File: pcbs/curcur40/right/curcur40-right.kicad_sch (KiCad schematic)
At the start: 88 parts, among them U1 PMW3360, U2 TLV74318PDBVR

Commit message: fix(pcb): eliminate all ERC/DRC/parity warnings and ignored DRC checks on left and right PCBs
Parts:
- U1: value PMW3360 -> PMW3360DM-T2QU; Mfr. # PMW3360DM-T2QU + LM19-LSI -> (none)
- rEXSW1: now left out of the parts list
- rLED9: footprint kbd_local:YS-SK6812MINI-E -> kbd_local:YS-SK6812MINI-E_rLED9
- rSW1: footprint kbd_local:keyswitch_choc12_hotswap_1u -> kbd_local:keyswitch_choc12_hotswap_1.5u
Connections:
- net +1V8_PMW: now also C1.1, C2.1, U1.3 (VDDPIX)
- net MOTION: no longer names the net of U1.9 (MOTION)
- no-connect marks 3 -> 4

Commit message: Refactor PCBs and schematics to use genuine KiCad 10.0 standard libraries and isolate PMW3360 VDDPIX
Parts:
- U1: footprint kbd_local:PMW3360DM-T2QU_16Pin -> kbd:PMW3360DM-T2QU_16Pin
- rEXLED2, rLED1, rLED10, rLED11, rLED12, rLED13, rLED14, rLED15, rLED16, rLED17, rLED18, rLED2, rLED3, rLED4, rLED5, rLED6, rLED7, rLED8: footprint kbd_local:YS-SK6812MINI-E -> kbd:YS-SK6812MINI-E; symbol kbd_local:YS-SK6812MINI-E -> kbd:YS-SK6812MINI-E
- rEXSW1: footprint kbd_local:CKW12 -> kbd:RotaryEncoder_Switch_CKW12
- rEXSW2, rSW10, rSW11, rSW12, rSW13, rSW14, rSW15, rSW16, rSW17, rSW18, rSW2, rSW3, rSW4, rSW5, rSW6, rSW7, rSW8, rSW9: footprint kbd_local:keyswitch_choc12_hotswap_1u -> kbd:keyswitch_choc12_hotswap_1u
- rJ1: footprint kbd_local:TYPE-C-31-M-13C -> kbd:USB_C_Receptacle_TYPE-C-31-M-13C; symbol Connector:USB_C_Receptacle_USB2.0 -> Connector:USB_C_Receptacle_USB2.0_16P
- rJ2: footprint kbd_local:PJ-398A-5A_PJ-399B-6A -> kbd:Jack_PJ-398A-5A_PJ-399B-6A
- rLED9: footprint kbd_local:YS-SK6812MINI-E_rLED9 -> kbd:YS-SK6812MINI-E_rLED9; symbol kbd_local:YS-SK6812MINI-E -> kbd:YS-SK6812MINI-E
- rSMDSW1, rSMDSW2: footprint kbd_local:TS-1088R-02026 -> kbd:TS-1088R-02026
- rSW1: footprint kbd_local:keyswitch_choc12_hotswap_1.5u -> kbd:keyswitch_choc12_hotswap_1.5u
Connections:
- net +1V8_PMW: no longer C1.1, C2.1, U1.3 (VDDPIX)
- net GNDR: now also rJ1.SH (SHIELD); no longer rJ1.S1 (SHIELD)
- new net: C1.1, C2.1, U1.3 (VDDPIX)
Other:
- moved on the sheet: rC1, rC2, rR3, rR4, rR5, rSMDSW2, rU4

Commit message: Clean up unused custom library files, fix fp-lib-table, and mark SWD headers J4/rJ4 as DNP
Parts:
- rJ4: now not fitted; now left out of the parts list
- rLED9: footprint kbd:YS-SK6812MINI-E_rLED9 -> kbd:YS-SK6812MINI-E
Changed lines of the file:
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@@
 			)
 		)
-		(property "Footprint" "kbd:YS-SK6812MINI-E_rLED9"
+		(property "Footprint" "kbd:YS-SK6812MINI-E"
 			(at 240.03 260.35 0)
 			(hide yes)
@@
 		(body_style 1)
 		(exclude_from_sim no)
-		(in_bom yes)
+		(in_bom no)
 		(on_board yes)
 		(in_pos_files yes)
-		(dnp no)
+		(dnp yes)
 		(fields_autoplaced yes)
 		(property "Reference" "rJ4"

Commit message: Unify SW1/rSW1 to 1u Choc footprint and document curcur40 component specs and sourcing in pcb_spec.md
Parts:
- rSW1: footprint kbd:keyswitch_choc12_hotswap_1.5u -> kbd:keyswitch_choc12_hotswap_1u
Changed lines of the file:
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@@
 			)
 		)
-		(property "Footprint" "kbd:keyswitch_choc12_hotswap_1.5u"
+		(property "Footprint" "kbd:keyswitch_choc12_hotswap_1u"
 			(at 248.92 148.59 0)
 			(hide yes)

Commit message: 1. 実施内容のまとめ
①・② 右手 PCB (curcur40-right) の JP1 直結化 ＆ R4 / C5 の DNP 化
JP1（電圧選択ジャンパ）の基板内パターン直結化:
curcur40-right.kicad_sch および curcur40-right.kicad_pcb の JP1 を、KiCad 10.0 標準のブリッジ済みシンボル・フットプリント（Jumper:SolderJumper_3_Bridged12 / Jumper:SolderJumper-3_P1.3mm_Bridged12_RoundedPad1.0x1.5mm_NumberLabels）に変更しました。
(net_tie_pad_groups "1, 2") と B.Cu 銅箔ポリゴンにより、Pad 1 (+3V3R) – Pad 2 (/V_{IO}) 間が最初から銅箔パターンで直結され、組み立て時のブリッジ忘れや逆ブリッジ（Pad 2–3 短絡）が物理的に起きない構造になっています。
R4 (28kΩ) と C5 (22nF) の DNP 化:
回路図・PCB の双方で DNP（未実装）・BOM 除外・CPL（実装座標）除外・3Dモデル非表示に設定しました。
あわせて、R1（10kΩ：/RESET プルアップ抵抗）に残っていた旧テンプレート由来の不要な dnp フラグを解除し、実装対象（C25804）として回路図・PCB・BOM/CPL の設定を統一しました。
１．ボトムプレートの削除・不要ファイルのクリーンアップ・スクリプト整理
ボトムプレート関連ファイルの完全削除:
plates/curcur40/pcb/plate-bottom* および plates/curcur40/pcb/jlcpcb/production_files/GERBER-plate-bottom* をすべて削除しました。
generate_plates.py およびレーザーカット用 plate-curcur40.svg からボトムプレート出力を削除し、左右トッププレートのみを出力するよう更新しました。
一時ファイル・スクラッチの削除:
scratch/, tmp/, .mypy_cache/, ルート直下の *_drc*.json, cases/curcur40/drc_check.rpt, cases/curcur40/right_pcb.step, 各 PCB/Plate フォルダ内の .rpt / .net / .bak* / .kicad_prl 等の作業用一時ファイルをすべて削除しました。
scripts/ フォルダの整理と格納ルールの策定:
恒久的に使用する公式ジェネレータ・エクスポータ 8本 に集約し、格納・運用ルールを scripts/README.md および pcb_spec.md 第9節 にまとめました：
generate_cases.py（左右ボトムケース STEP/STL 生成）
generate_trackball_cup.py（トラックボールカップ＆ボール付アセンブリ STEP/STL 生成）
generate_sensor_assemblies.py（光学センサー検証用 STEP 2種生成）
generate_full_assembly.py（フルアセンブリ STEP 生成＆全干渉検証）
generate_plates.py（左右トッププレート PCB/SVG 生成＆DRC検証）
export_jlcpcb.py（JLCPCB 発注用 Gerber ZIP / BOM CSV / CPL CSV 一括出力）
generate_spec_diagrams.py（仕様書用の断面・解説図版生成）
render_previews.py（ドキュメント用 3D プレビュー画像一括レンダリング）
２．4つの 3D モデル（STEP）へのレンズ側光学距離基準点のプロット

GUI（CAD Viewer 等）の計測ツール（📏 Measure）で直接クリック選択し、25mm ボール球面（Trackball_25mm, 最下面
𝑍
rel
=
+
5.80
 mm
Z
rel
	​

=+5.80 mm）との最短距離を計測した際に正確に設計値 2.40 mm が表示されるよう、光軸中心
(
𝑋
opt
,
𝑌
opt
)
(X
opt
	​

,Y
opt
	​

) のレンズフランジ着座高さ（
𝑍
rel
=
+
3.4000
 mm
Z
rel
	​

=+3.4000 mm / フルアセンブリ
𝑍
=
−
0.2000
 mm
Z=−0.2000 mm）に独立した名前付きオブジェクト Lens_Optical_Ref_Point（厚みゼ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
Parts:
- C5, R4: now left out of the parts list
- JP1: value SolderJumper_3_Open -> SolderJumper_3_Bridged12; footprint Jumper:SolderJumper-3_P1.3mm_Open_RoundedPad1.0x1.5mm_NumberLabels -> Jumper:SolderJumper-3_P1.3mm_Bridged12_RoundedPad1.0x1.5mm_NumberLabels; symbol Jumper:SolderJumper_3_Open -> Jumper:SolderJumper_3_Bridged12
- R1: now fitted
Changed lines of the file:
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@@
 		(body_style 1)
 		(exclude_from_sim no)
-		(in_bom yes)
+		(in_bom no)
 		(on_board yes)
-		(in_pos_files yes)
+		(in_pos_files no)
 		(dnp yes)
 		(property "Reference" "C5"
@@
 		(body_style 1)
 		(exclude_from_sim no)
-		(in_bom yes)
+		(in_bom no)
 		(on_board yes)
-		(in_pos_files yes)
+		(in_pos_files no)
 		(dnp yes)
 		(property "Reference" "R4"
@@
 	)
 (symbol
-		(lib_id "Jumper:SolderJumper_3_Open")
+		(lib_id "Jumper:SolderJumper_3_Bridged12")
 		(at 385.00 177.39 90)
 		(unit 1)
@@
 			)
 		)
-		(property "Value" "SolderJumper_3_Open"
+		(property "Value" "SolderJumper_3_Bridged12"
 			(at 378.65 177.39 0)
 			(hide yes)
@@
 			)
 		)
-		(property "Footprint" "Jumper:SolderJumper-3_P1.3mm_Open_RoundedPad1.0x1.5mm_NumberLabels"
+		(property "Footprint" "Jumper:SolderJumper-3_P1.3mm_Bridged12_RoundedPad1.0x1.5mm_NumberLabels"
 			(at 385.00 177.39 0)
 			(hide yes)
@@
 			)
 		)
-		(property "Description" "Solder Jumper, 3-pole, open"
+		(property "Description" "3-pole Solder Jumper, pins 1+2 closed/bridged"
 			(at 385.00 177.39 0)
 			(show_name no)
@@
 		(on_board yes)
 		(in_pos_files yes)
-		(dnp yes)
+		(dnp no)
 		(property "Reference" "R1"
 			(at 352.88 79.61 0)

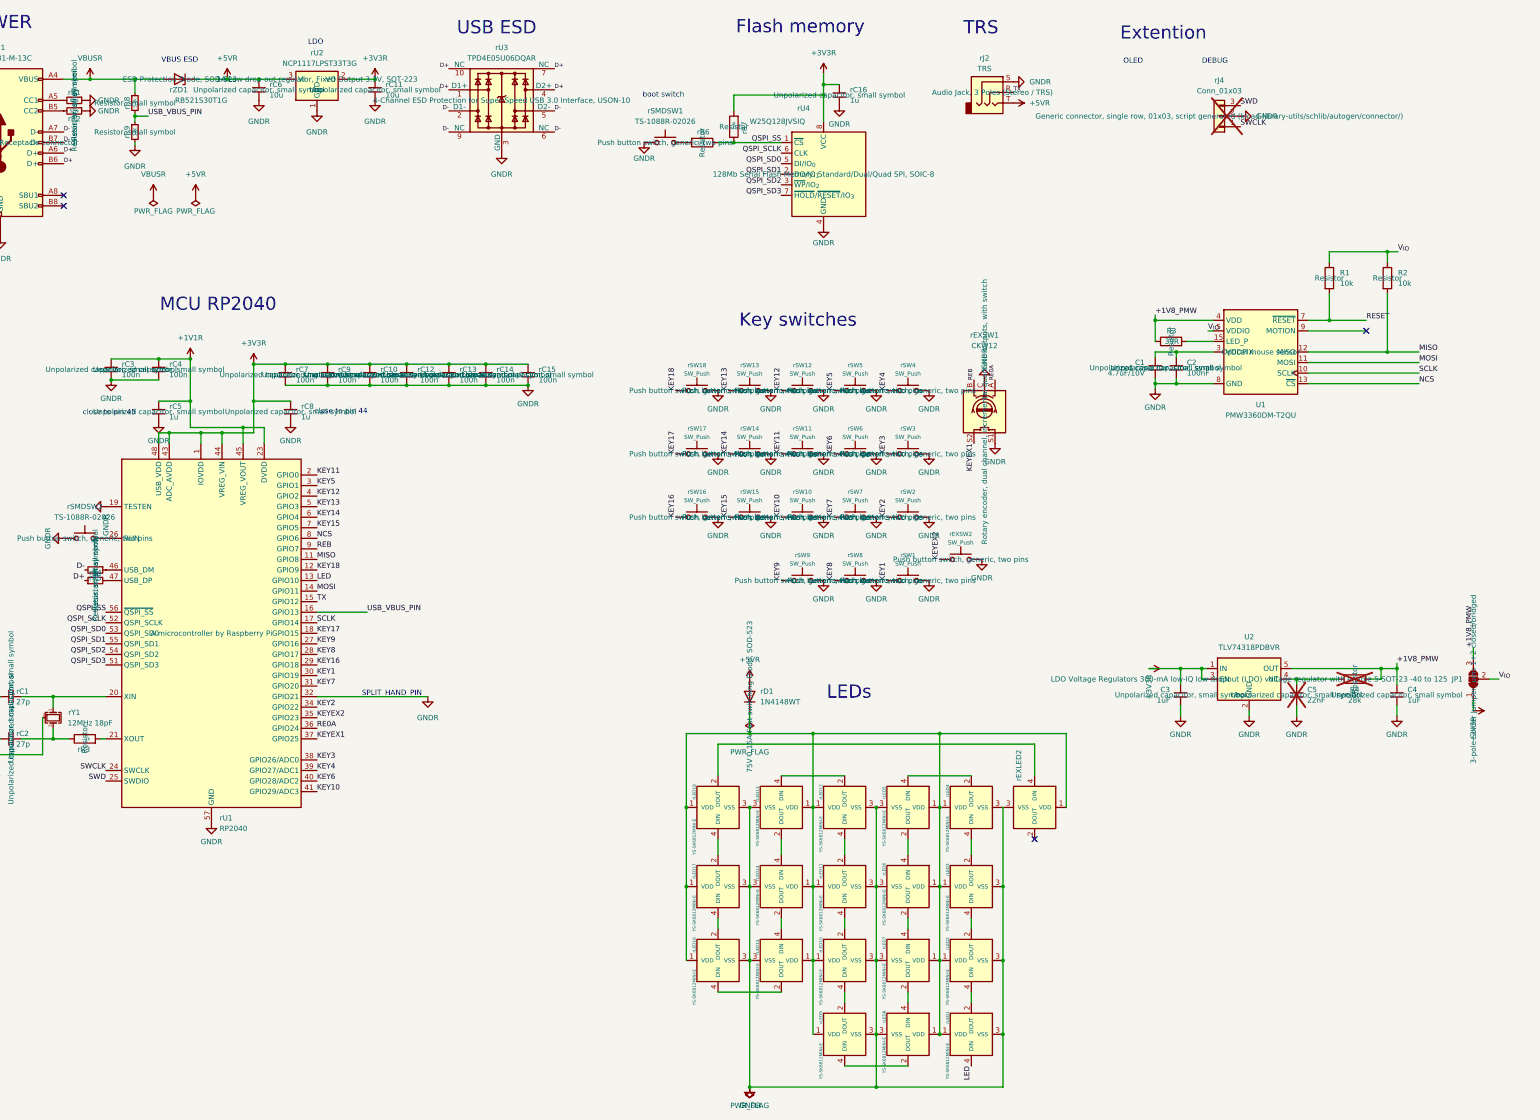
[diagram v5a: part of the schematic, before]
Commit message: fix(pcb): resolve all ERC off-grid/four-way-junction warnings and restore PCB symbol UUID paths
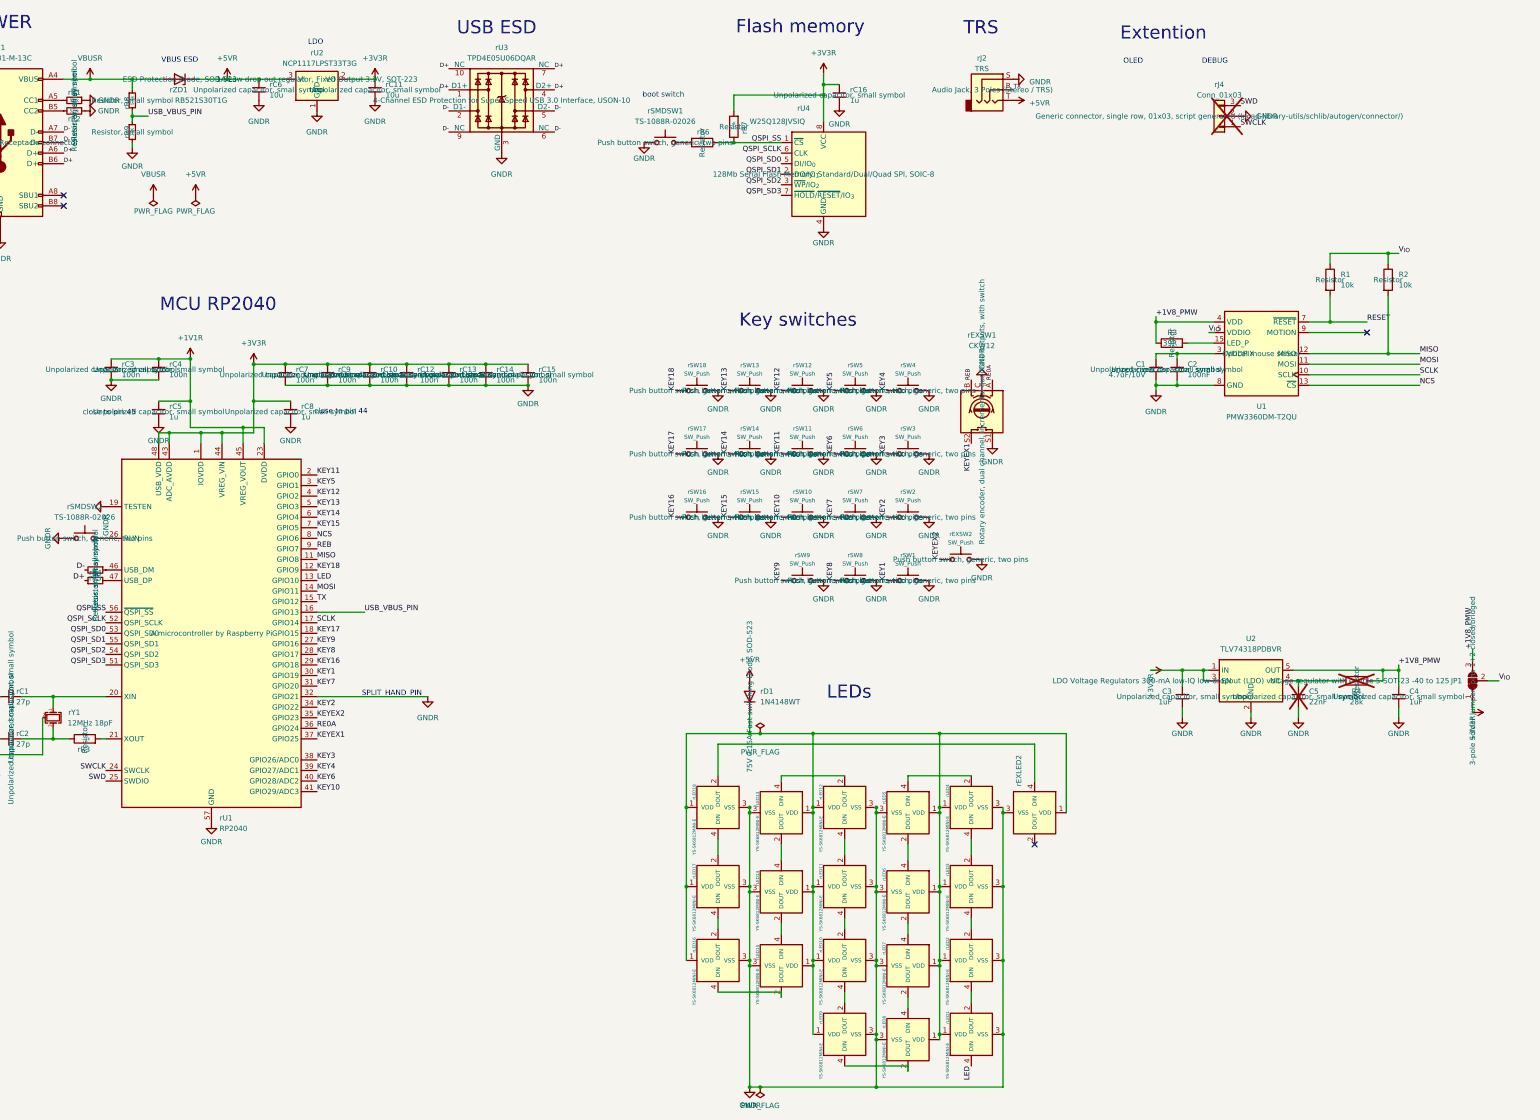
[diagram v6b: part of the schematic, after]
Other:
- moved on the sheet: C3, C4, C5, R4, U2, rEXLED2, rEXSW1, rJ2, rLED13, rLED14, rLED15, rLED5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
